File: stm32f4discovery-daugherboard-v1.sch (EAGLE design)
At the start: 41 parts

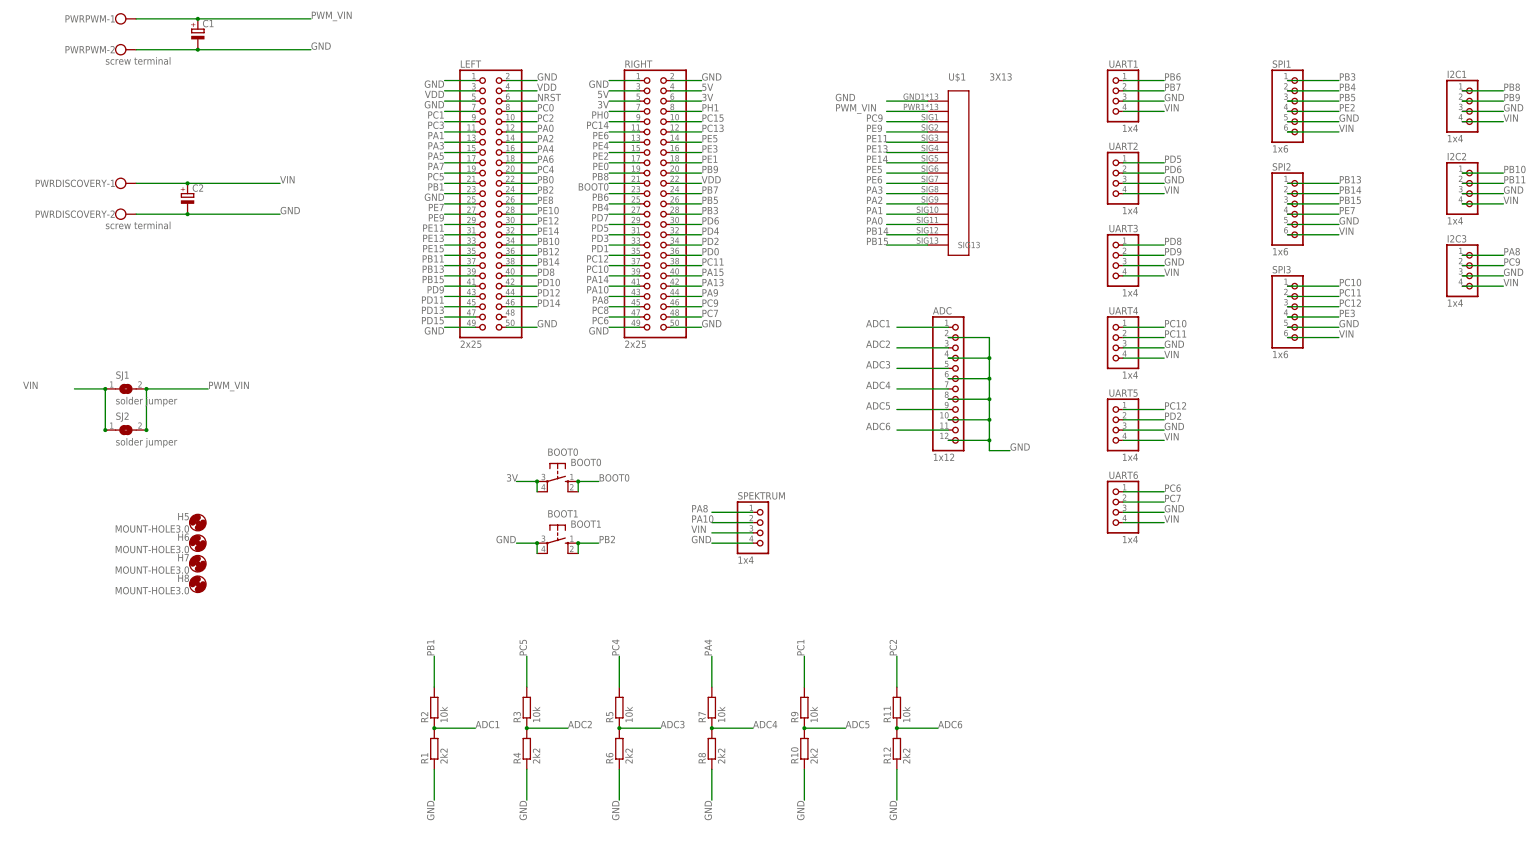
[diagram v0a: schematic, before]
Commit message: replaced v1 with v2
deleted v1, renamed v2 to v1
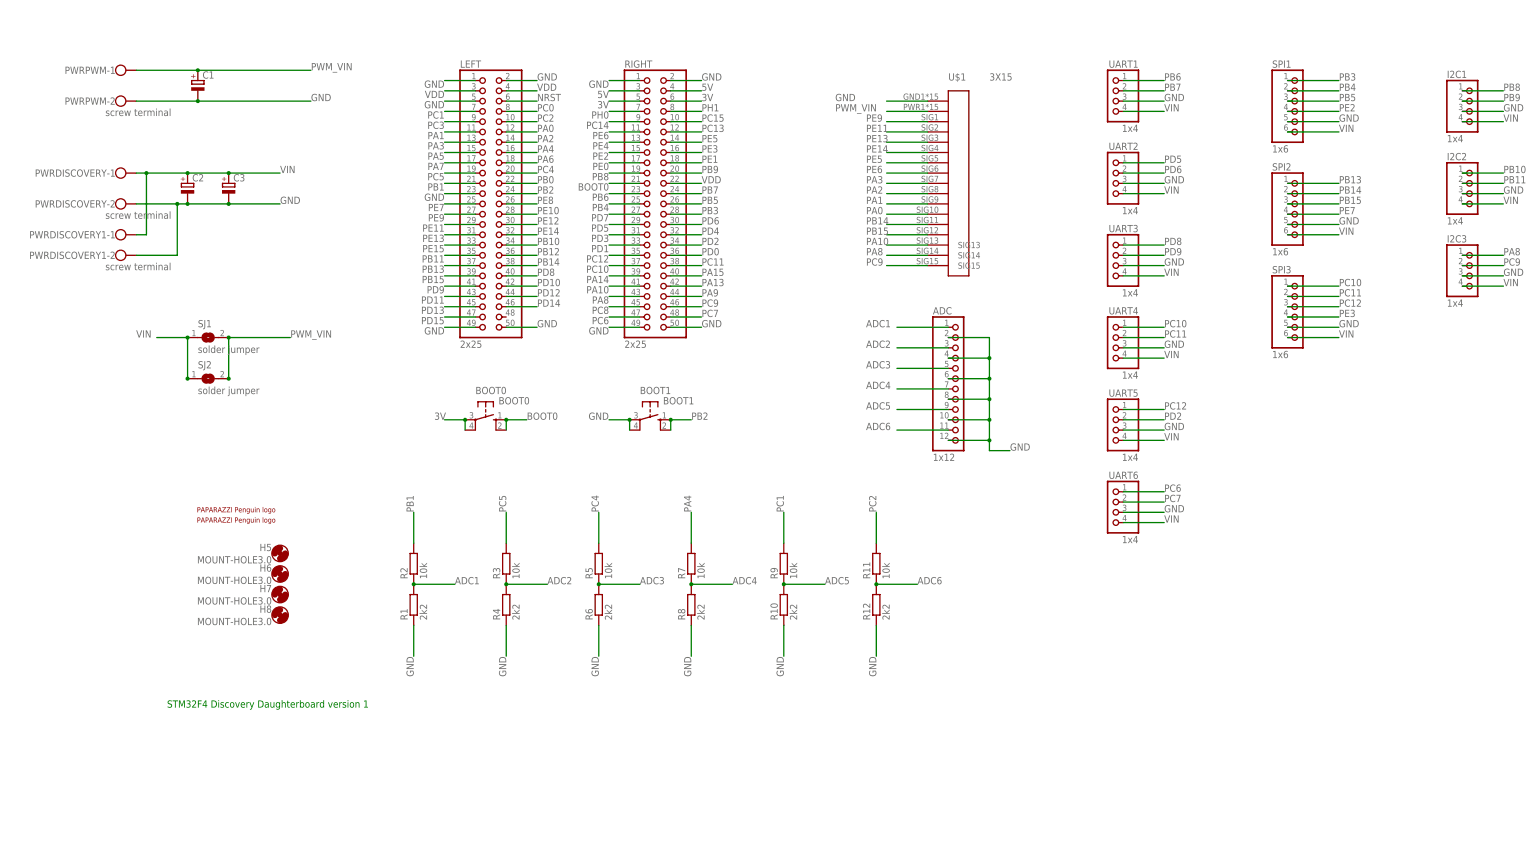
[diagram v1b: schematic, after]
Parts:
- removed SPEKTRUM: 1x4, pinhead:PINHD-1X4/90
- added C3: (no value), rcl:CPOL-EU153CLV-0807
- added PWRDISCOVERY1: screw terminal, con-wago-500:W237-102
- added U$2, U$3: PAPARAZZI, paparazzi:PAPARAZZI
- U$1: value 3X13 -> 3X15; device pinhead3:3X13 -> pinhead3:3X15
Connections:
- net GND: now also C3.-, PWRDISCOVERY1-2.KL; no longer SPEKTRUM.4
- net PA0: now also U$1.SIG10; no longer U$1.SIG11
- net PA1: now also U$1.SIG9; no longer U$1.SIG10
- net PA10: now also U$1.SIG13; no longer SPEKTRUM.2
- net PA2: now also U$1.SIG8; no longer U$1.SIG9
- net PA3: now also U$1.SIG7; no longer U$1.SIG8
- net PA8: now also U$1.SIG14; no longer SPEKTRUM.1
- net PB14: now also U$1.SIG11; no longer U$1.SIG12
- net PB15: now also U$1.SIG12; no longer U$1.SIG13
- net PC9: now also U$1.SIG15; no longer U$1.SIG1
- net PE11: now also U$1.SIG2; no longer U$1.SIG3
- net PE13: now also U$1.SIG3; no longer U$1.SIG4
- net PE14: now also U$1.SIG4; no longer U$1.SIG5
- net PE5: now also U$1.SIG5; no longer U$1.SIG6
- net PE6: now also U$1.SIG6; no longer U$1.SIG7
- net PE9: now also U$1.SIG1; no longer U$1.SIG2
- net VIN: now also C3.+, PWRDISCOVERY1-1.KL; no longer SPEKTRUM.3
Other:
- note added: "STM32F4 Discovery Daughterboard version 1"
- moved on the sheet: BOOT0, BOOT1, C1, C2, H5, H6, H7, H8, PWRDISCOVERY-1, PWRDISCOVERY-2, PWRPWM-1, PWRPWM-2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

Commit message: updated
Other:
- note added: "In most cases, BOOT1 is not needed"
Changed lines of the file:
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@@
 <plain>
 <text x="-111.76" y="-83.82" size="1.778" layer="91">STM32F4 Discovery Daughterboard version 1</text>
+<text x="-10.16" y="-20.32" size="1.778" layer="91">In most cases, BOOT1 is not needed</text>
 </plain>
 <instances>

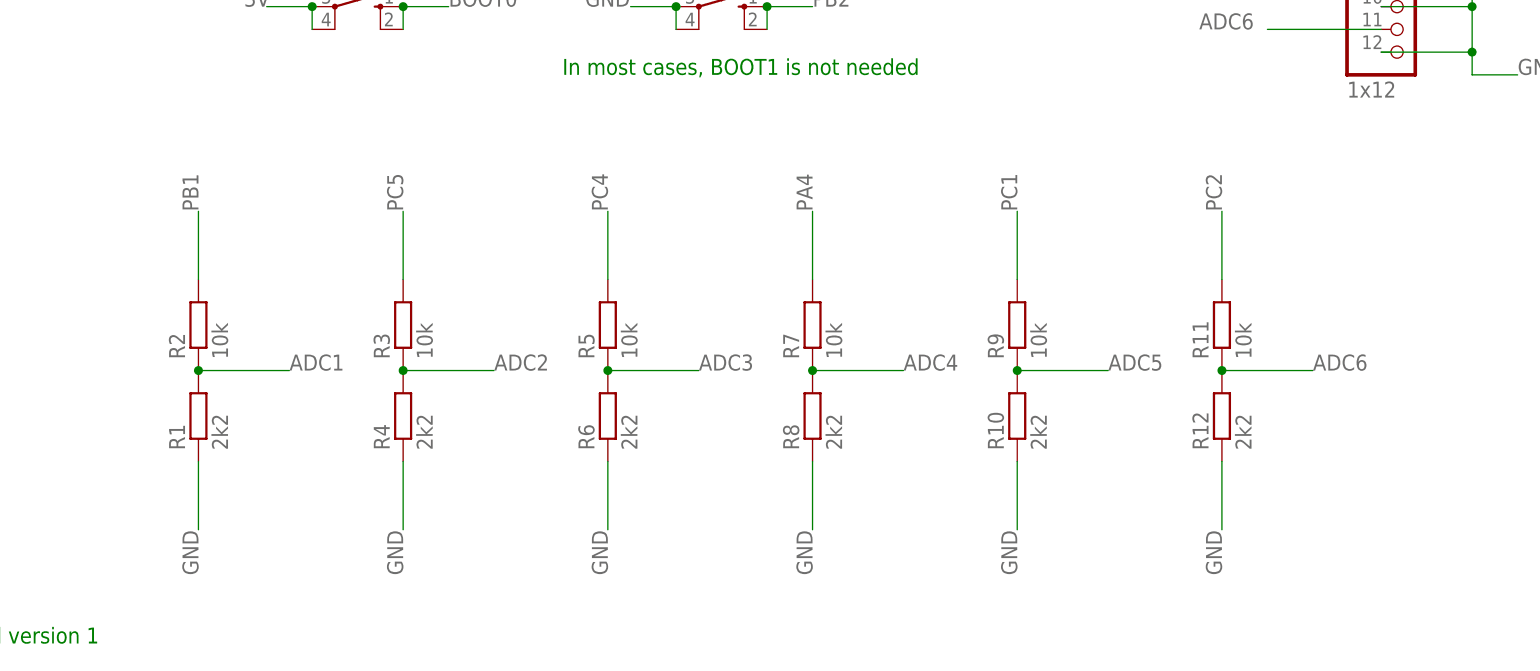
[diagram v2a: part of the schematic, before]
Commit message: corrected adc voltage divider
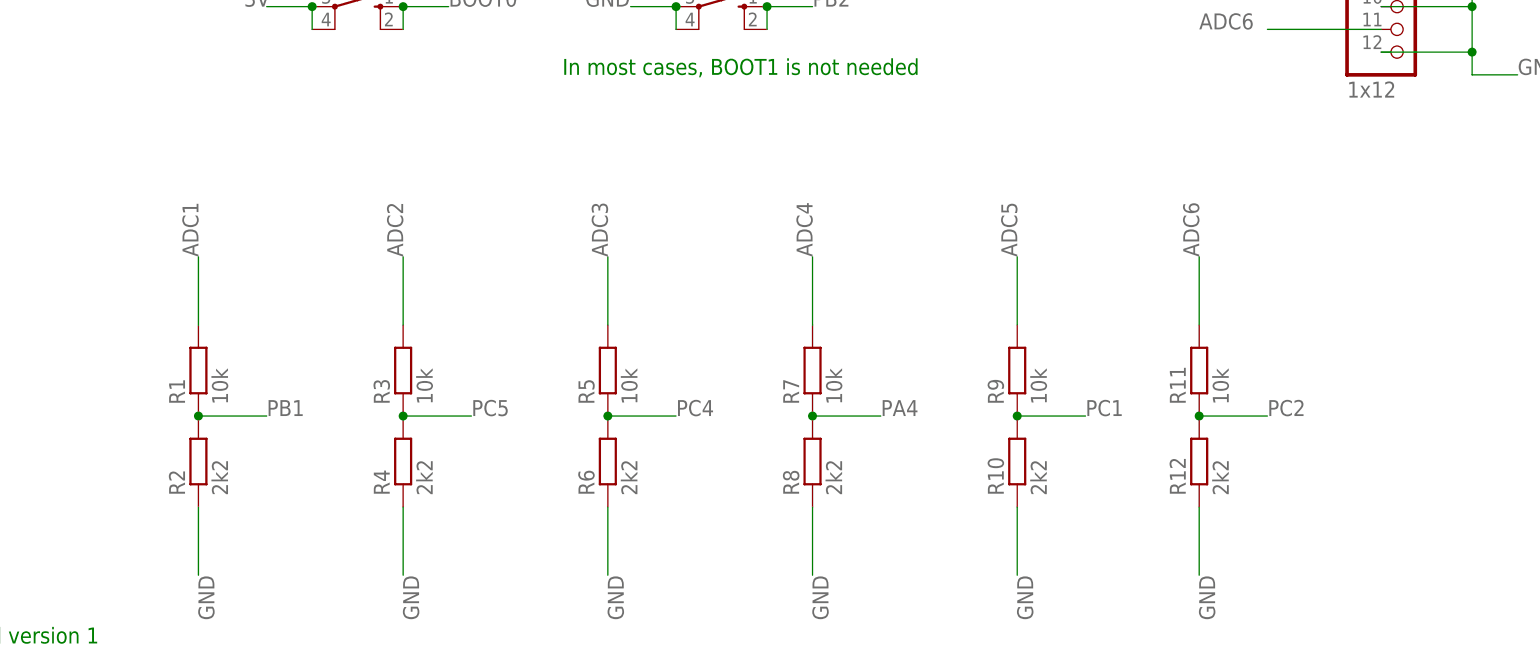
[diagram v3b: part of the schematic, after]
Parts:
- R1: value 2k2 -> 10k; device resistor:R-EU_M0805 -> rcl:R-EU_R0805
- R10, R11, R12, R3, R4, R5, R6, R7, R8, R9: device resistor:R-EU_M0805 -> rcl:R-EU_R0805
- R2: value 10k -> 2k2; device resistor:R-EU_M0805 -> rcl:R-EU_R0805
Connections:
- net ADC1: no longer R2.1
- net ADC2: now also R3.2; no longer R3.1, R4.2
- net ADC3: now also R5.2; no longer R5.1, R6.2
- net ADC4: now also R7.2; no longer R7.1, R8.2
- net ADC5: now also R9.2; no longer R10.2, R9.1
- net ADC6: now also R11.2; no longer R11.1, R12.2
- net GND: now also R2.1; no longer R1.1
- net PA4: now also R7.1, R8.2; no longer R7.2
- net PB1: now also R1.1
- net PC1: now also R10.2, R9.1; no longer R9.2
- net PC2: now also R11.1, R12.2; no longer R11.2
- net PC4: now also R5.1, R6.2; no longer R5.2
- net PC5: now also R3.1, R4.2; no longer R3.2
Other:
- moved on the sheet: R1, R10, R11, R12, R2, R3, R4, R5, R6, R7, R8, R9

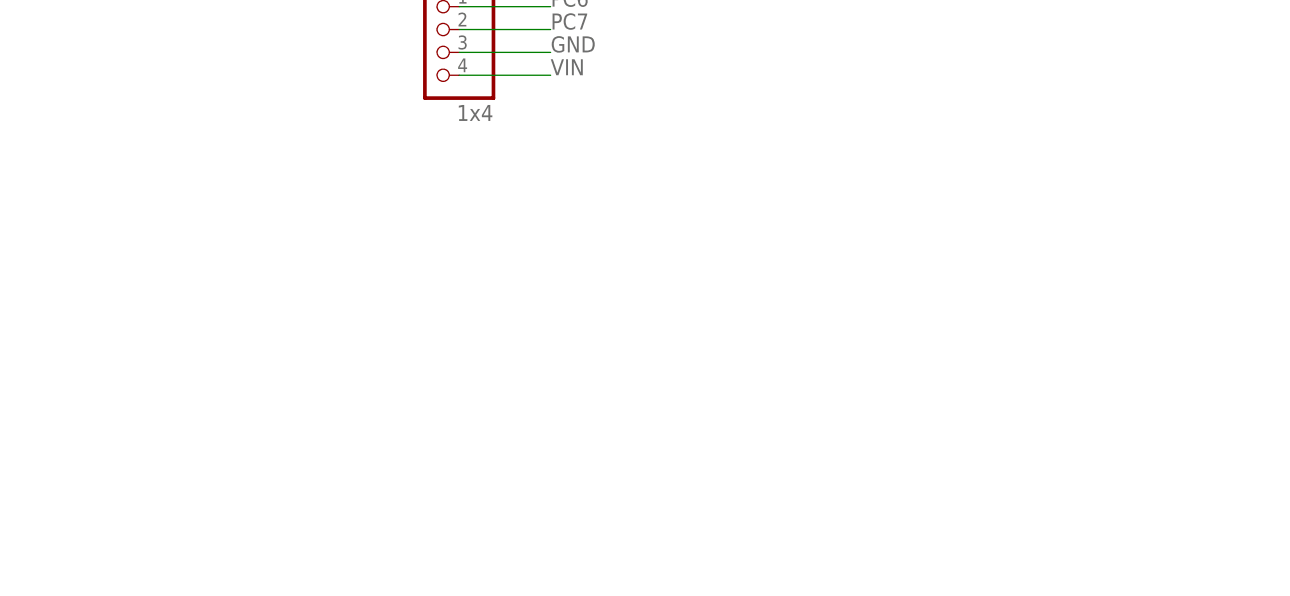
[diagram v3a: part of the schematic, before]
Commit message: added suppressor diode on all adc
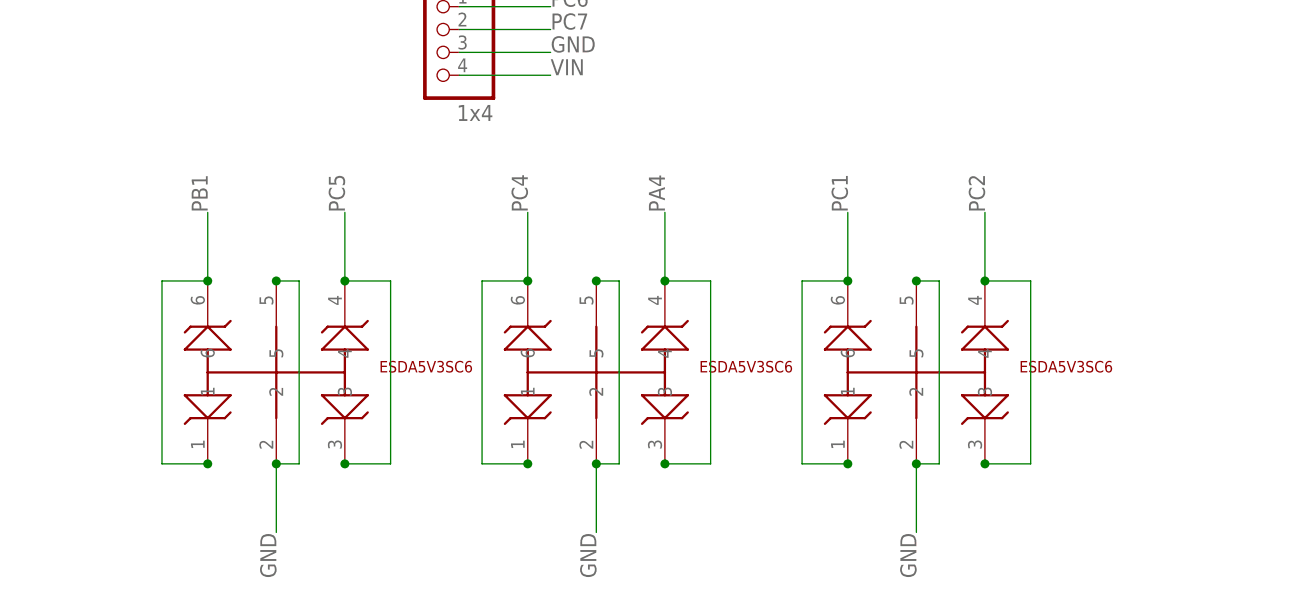
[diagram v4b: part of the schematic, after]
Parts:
- added U$4, U$5, U$6: ESDA5V3SC6, suppressor diode:ESDA5V3SC6
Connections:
- net GND: now also U$4.2, U$4.5, U$5.2, U$5.5, U$6.2, U$6.5
- net PA4: now also U$5.3, U$5.4
- net PB1: now also U$4.1, U$4.6
- net PC1: now also U$6.1, U$6.6
- net PC2: now also U$6.3, U$6.4
- net PC4: now also U$5.1, U$5.6
- net PC5: now also U$4.3, U$4.4
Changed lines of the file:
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@@
 <part name="R11" library="rcl" deviceset="R-EU_" device="R0805" value="10k"/>
 <part name="R12" library="rcl" deviceset="R-EU_" device="R0805" value="2k2"/>
+<part name="U$4" library="suppressor diode" deviceset="ESDA5V3SC6" device=""/>
+<part name="U$5" library="suppressor diode" deviceset="ESDA5V3SC6" device=""/>
+<part name="U$6" library="suppressor diode" deviceset="ESDA5V3SC6" device=""/>
 </parts>
 <sheets>
@@
 <instance part="R11" gate="G$1" x="60.96" y="-53.34" rot="R90"/>
 <instance part="R12" gate="G$1" x="60.96" y="-63.5" rot="R90"/>
+<instance part="U$4" gate="G$1" x="104.14" y="-71.12"/>
+<instance part="U$5" gate="G$1" x="139.7" y="-71.12"/>
+<instance part="U$6" gate="G$1" x="175.26" y="-71.12"/>
 </instances>
 <busses>
@@
 <label x="60.96" y="-76.2" size="1.778" layer="95" rot="R270"/>
 </segment>
+<segment>
+<pinref part="U$4" gate="G$1" pin="2"/>
+<wire x1="104.14" y1="-81.28" x2="104.14" y2="-88.9" width="0.1524" layer="91"/>
+<pinref part="U$4" gate="G$1" pin="5"/>
+<wire x1="104.14" y1="-60.96" x2="106.68" y2="-60.96" width="0.1524" layer="91"/>
+<wire x1="106.68" y1="-60.96" x2="106.68" y2="-81.28" width="0.1524" layer="91"/>
+<wire x1="106.68" y1="-81.28" x2="104.14" y2="-81.28" width="0.1524" layer="91"/>
+<junction x="104.14" y="-81.28"/>
+<junction x="104.14" y="-60.96"/>
+<label x="104.14" y="-93.98" size="1.778" layer="95" rot="R90"/>
+</segment>
+<segment>
+<pinref part="U$5" gate="G$1" pin="2"/>
+<wire x1="139.7" y1="-81.28" x2="139.7" y2="-88.9" width="0.1524" layer="91"/>
+<pinref part="U$5" gate="G$1" pin="5"/>
+<wire x1="139.7" y1="-60.96" x2="142.24" y2="-60.96" width="0.1524" layer="91"/>
+<wire x1="142.24" y1="-60.96" x2="142.24" y2="-81.28" width="0.1524" layer="91"/>
+<wire x1="142.24" y1="-81.28" x2="139.7" y2="-81.28" width="0.1524" layer="91"/>
+<junction x="139.7" y="-81.28"/>
+<junction x="139.7" y="-60.96"/>
+<label x="139.7" y="-93.98" size="1.778" layer="95" rot="R90"/>
+</segment>
+<segment>
+<pinref part="U$6" gate="G$1" pin="2"/>
+<wire x1="175.26" y1="-81.28" x2="175.26" y2="-88.9" width="0.1524" layer="91"/>
+<pinref part="U$6" gate="G$1" pin="5"/>
+<wire x1="175.26" y1="-60.96" x2="177.8" y2="-60.96" width="0.1524" layer="91"/>
+<wire x1="177.8" y1="-60.96" x2="177.8" y2="-81.28" width="0.1524" layer="91"/>
+<wire x1="177.8" y1="-81.28" x2="175.26" y2="-81.28" width="0.1524" layer="91"/>
+<junction x="175.26" y="-81.28"/>
+<junction x="175.26" y="-60.96"/>
+<label x="175.26" y="-93.98" size="1.778" layer="95" rot="R90"/>
+</segment>
 </net>
 <net name="VDD" class="0">
@@
 <junction x="40.64" y="-58.42"/>
 </segment>
+<segment>
+<pinref part="U$6" gate="G$1" pin="6"/>
+<wire x1="167.64" y1="-60.96" x2="167.64" y2="-53.34" width="0.1524" layer="91"/>
+<pinref part="U$6" gate="G$1" pin="1"/>
+<wire x1="167.64" y1="-81.28" x2="162.56" y2="-81.28" width="0.1524" layer="91"/>
+<wire x1="162.56" y1="-81.28" x2="162.56" y2="-60.96" width="0.1524" layer="91"/>
+<wire x1="162.56" y1="-60.96" x2="167.64" y2="-60.96" width="0.1524" layer="91"/>
+<junction x="167.64" y="-60.96"/>
+<junction x="167.64" y="-81.28"/>
+<label x="167.64" y="-53.34" size="1.778" layer="95" rot="R90"/>
+</segment>
 </net>
 <net name="PA1" class="0">
@@
 <junction x="-27.94" y="-58.42"/>
 </segment>
+<segment>
+<pinref part="U$4" gate="G$1" pin="4"/>
+<wire x1="111.76" y1="-60.96" x2="111.76" y2="-53.34" width="0.1524" layer="91"/>
+<pinref part="U$4" gate="G$1" pin="3"/>
+<wire x1="111.76" y1="-81.28" x2="116.84" y2="-81.28" width="0.1524" layer="91"/>
+<wire x1="116.84" y1="-81.28" x2="116.84" y2="-60.96" width="0.1524" layer="91"/>
+<wire x1="116.84" y1="-60.96" x2="111.76" y2="-60.96" width="0.1524" layer="91"/>
+<junction x="111.76" y="-60.96"/>
+<junction x="111.76" y="-81.28"/>
+<label x="111.76" y="-53.34" size="1.778" layer="95" rot="R90"/>
+</segment>
 </net>
 <net name="PB1" class="0">
@@
 <junction x="-50.8" y="-58.42"/>
 </segment>
+<segment>
+<pinref part="U$4" gate="G$1" pin="6"/>
+<wire x1="96.52" y1="-60.96" x2="96.52" y2="-53.34" width="0.1524" layer="91"/>
+<pinref part="U$4" gate="G$1" pin="1"/>
+<wire x1="96.52" y1="-81.28" x2="91.44" y2="-81.28" width="0.1524" layer="91"/>
+<wire x1="91.44" y1="-81.28" x2="91.44" y2="-60.96" width="0.1524" layer="91"/>
+<wire x1="91.44" y1="-60.96" x2="96.52" y2="-60.96" width="0.1524" layer="91"/>
+<junction x="96.52" y="-60.96"/>
+<junction x="96.52" y="-81.28"/>
+<label x="96.52" y="-53.34" size="1.778" layer="95" rot="R90"/>
+</segment>
 </net>
 <net name="PE7" class="0">
@@
 <junction x="60.96" y="-58.42"/>
 </segment>
+<segment>
+<pinref part="U$6" gate="G$1" pin="4"/>
+<wire x1="182.88" y1="-60.96" x2="182.88" y2="-53.34" width="0.1524" layer="91"/>
+<pinref part="U$6" gate="G$1" pin="3"/>
+<wire x1="182.88" y1="-81.28" x2="187.96" y2="-81.28" width="0.1524" layer="91"/>
+<wire x1="187.96" y1="-81.28" x2="187.96" y2="-60.96" width="0.1524" layer="91"/>
+<wire x1="187.96" y1="-60.96" x2="182.88" y2="-60.96" width="0.1524" layer="91"/>
+<junction x="182.88" y="-60.96"/>
+<junction x="182.88" y="-81.28"/>
+<label x="182.88" y="-53.34" size="1.778" layer="95" rot="R90"/>
+</segment>
 </net>
 <net name="PA2" class="0">
@@
 <pinref part="R6" gate="G$1" pin="2"/>
 <junction x="-5.08" y="-58.42"/>
+</segment>
+<segment>
+<pinref part="U$5" gate="G$1" pin="6"/>
+<wire x1="132.08" y1="-60.96" x2="132.08" y2="-53.34" width="0.1524" layer="91"/>
+<pinref part="U$5" gate="G$1" pin="1"/>
+<wire x1="132.08" y1="-81.28" x2="127" y2="-81.28" width="0.1524" layer="91"/>
+<wire x1="127" y1="-81.28" x2="127" y2="-60.96" width="0.1524" layer="91"/>
+<wire x1="127" y1="-60.96" x2="132.08" y2="-60.96" width="0.1524" layer="91"/>
+<junction x="132.08" y="-60.96"/>
+<junction x="132.08" y="-81.28"/>
+<label x="132.08" y="-53.34" size="1.778" layer="95" rot="R90"/>
 </segment>
 </net>
@@
 <junction x="17.78" y="-58.42"/>
 </segment>
-</net>
+<segment>
+<pinref part="U$5" gate="G$1" pin="4"/>
+<wire x1="147.32" y1="-60.96" x2="147.32" y2="-53.34" width="0.1524" layer="91"/>
+<pinref part="U$5" gate="G$1" pin="3"/>
+<wire x1="147.32" y1="-81.28" x2="152.4" y2="-81.28" width="0.1524" layer="91"/>
+<wire x1="152.4" y1="-81.28" x2="152.4" y2="-60.96" width="0.1524" layer="91"/>
+<wire x1="152.4" y1="-60.96" x2="147.32" y2="-60.96" width="0.1524" layer="91"/>
+<junction x="147.32" y="-81.28"/>
+<junction x="147.32" y="-60.96"/>
+<label x="147.32" y="-53.34" size="1.778" layer="95" rot="R90"/>
+</segment>
+</net>

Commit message: input protection
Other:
- note added: "this version is not up to date, look at the tht version !!!"
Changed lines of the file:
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@@
 <text x="-111.76" y="-83.82" size="1.778" layer="91">STM32F4 Discovery Daughterboard version 1</text>
 <text x="-10.16" y="-20.32" size="1.778" layer="91">In most cases, BOOT1 is not needed</text>
+<text x="-109.22" y="-114.3" size="6.4516" layer="91">this version is not up to date, look at the tht version !!!</text>
 </plain>
 <instances>
